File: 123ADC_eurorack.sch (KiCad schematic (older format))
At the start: 78 parts, among them J1 CLOCK_IN, J10 BIT_7, J11 Conn_01x06_Male, J12 Conn_01x06_Female, J13 Conn_01x06_Male, J14 Conn_01x06_Female, J15 Conn_02x05_Odd_Even, J2 CV_IN, J3 BIT_0, J4 BIT_1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

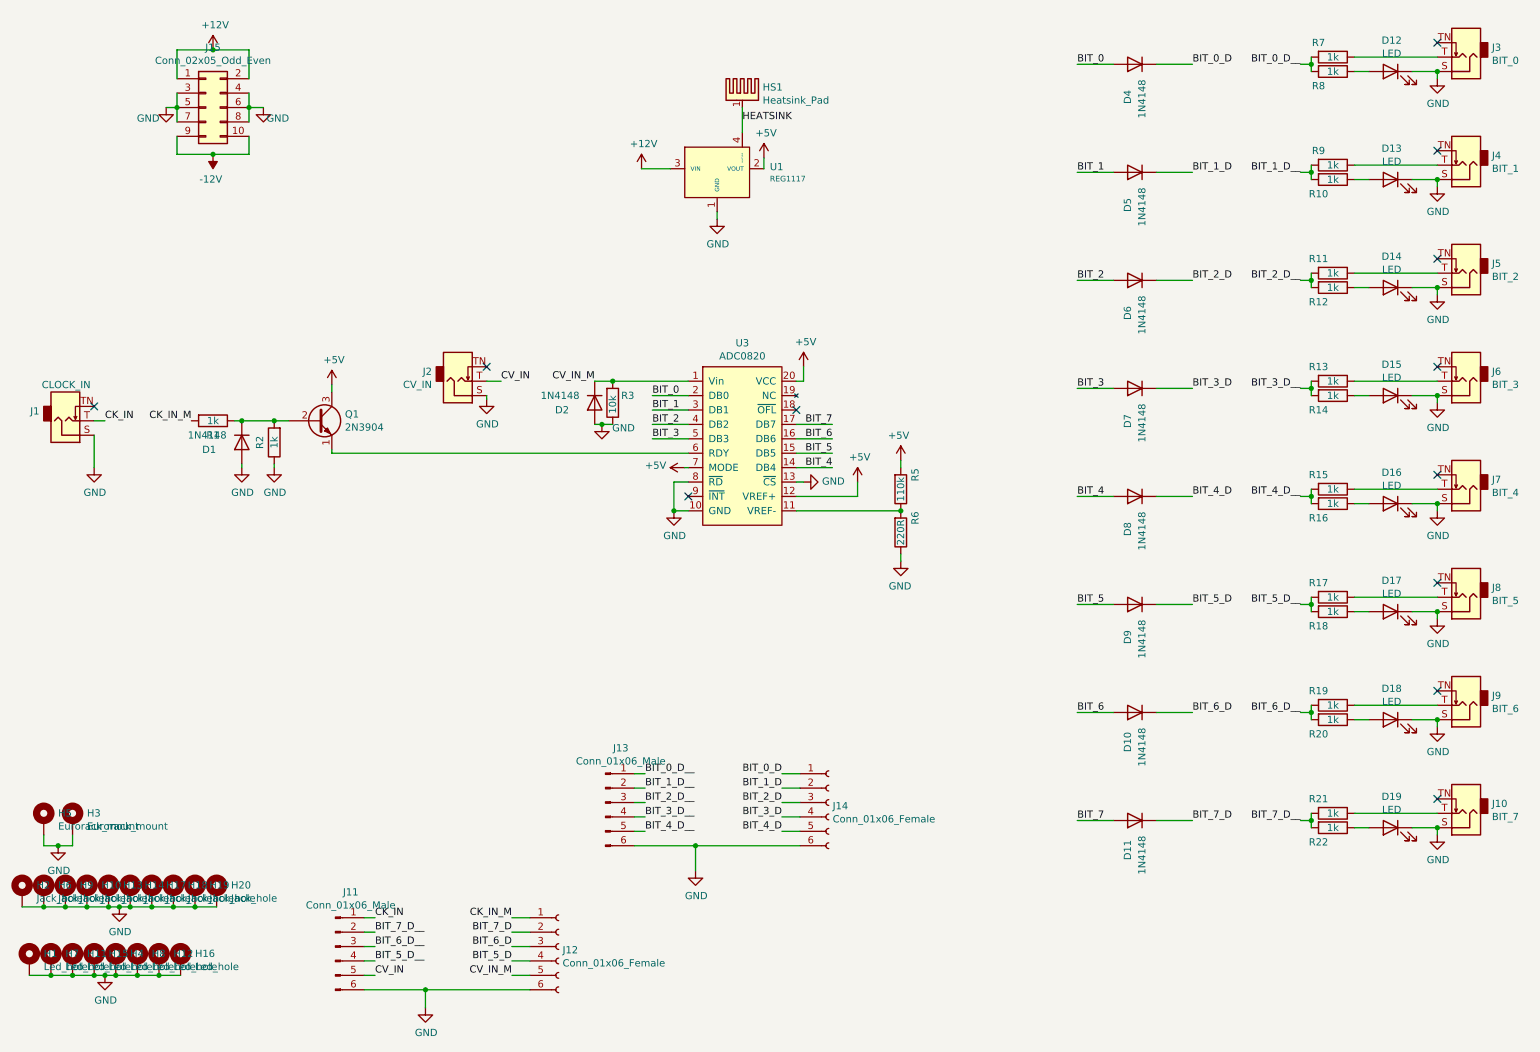
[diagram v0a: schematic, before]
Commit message: :sparkles: Add reverse power protection and power conditioning caps
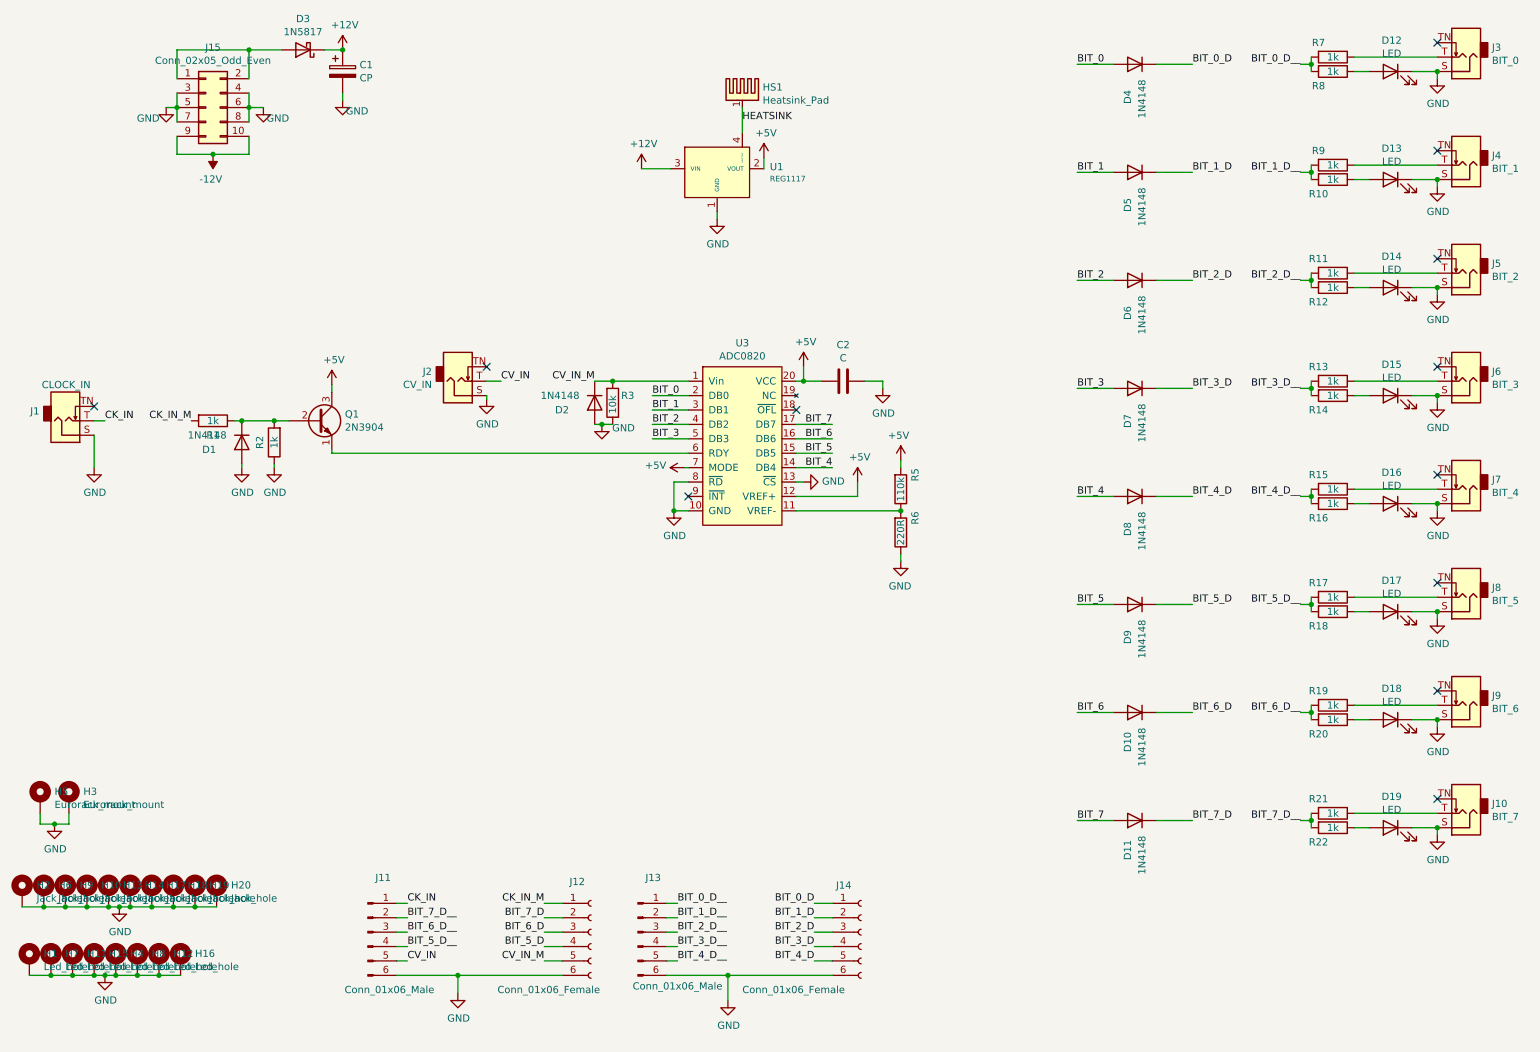
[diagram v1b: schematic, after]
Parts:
- added C1: CP, Capacitor_THT:CP_Radial_D5.0mm_P2.50mm, symbol Device:CP
- added C2: C, Capacitor_THT:C_Disc_D3.8mm_W2.6mm_P2.50mm, symbol Device:C
- added D3: 1N5817, Diode_THT:D_DO-41_SOD81_P10.16mm_Horizontal, symbol Diode:1N5817
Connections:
- net +12V: now also C1.1, D3.1 (K); no longer J15.1 (Pin_1), J15.2 (Pin_2)
- net +5V: now also C2.2
- net GND: now also C1.2, C2.1
- new net: D3.2 (A), J15.1 (Pin_1), J15.2 (Pin_2)
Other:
- moved on the sheet: H3, H5, J11, J12, J13, J14

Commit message: :bug: Fix resistor values
same
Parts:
- C1: symbol Device:CP -> 123ADC_eurorack-rescue:CP-Device
- Q1: footprint Package_TO_SOT_THT:TO-92_Inline -> Package_TO_SOT_THT:TO-92_Inline_Wide
- R10, R12, R14, R16, R18, R2, R20, R22, R8: value 1k -> 10k
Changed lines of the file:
@@
 EESchema Schematic File Version 4
-EELAYER 26 0
+EELAYER 30 0
 EELAYER END
 $Descr A4 11693 8268
@@
 P 9725 1675
 F 0 "R10" V 9825 1575 50  0000 C CNN
-F 1 "1k" V 9725 1675 50  0000 C CNN
+F 1 "10k" V 9725 1675 50  0000 C CNN
 F 2 "Resistor_THT:R_Axial_DIN0207_L6.3mm_D2.5mm_P7.62mm_Horizontal" V 9655 1675 50  0001 C CNN
 F 3 "~" H 9725 1675 50  0001 C CNN
@@
 F 0 "Q1" H 2866 3396 50  0000 L CNN
 F 1 "2N3904" H 2866 3305 50  0000 L CNN
-F 2 "Package_TO_SOT_THT:TO-92_Inline" H 2875 3275 50  0001 L CIN
+F 2 "Package_TO_SOT_THT:TO-92_Inline_Wide" H 2875 3275 50  0001 L CIN
 F 3 "https://www.fairchildsemi.com/datasheets/2N/2N3904.pdf" H 2675 3350 50  0001 L CNN
 	1    2675 3350
@@
 P 2150 3500
 F 0 "D1" V 2200 3775 50  0000 R CNN
-F 1 "1N4148" V 2100 3875 50  0000 R CNN
+F 1 "1N4148" V 2325 3875 50  0000 R CNN
 F 2 "Diode_THT:D_DO-35_SOD27_P7.62mm_Horizontal" H 2150 3325 50  0001 C CNN
 F 3 "https://assets.nexperia.com/documents/data-sheet/1N4148_1N4448.pdf" H 2150 3500 50  0001 C CNN
@@
 P 2375 3500
 F 0 "R2" V 2475 3500 50  0000 C CNN
-F 1 "1k" V 2375 3500 50  0000 C CNN
+F 1 "10k" V 2375 3500 50  0000 C CNN
 F 2 "Resistor_THT:R_Axial_DIN0207_L6.3mm_D2.5mm_P7.62mm_Horizontal" V 2305 3500 50  0001 C CNN
 F 3 "~" H 2375 3500 50  0001 C CNN
@@
 P 9725 2425
 F 0 "R12" V 9825 2325 50  0000 C CNN
-F 1 "1k" V 9725 2425 50  0000 C CNN
+F 1 "10k" V 9725 2425 50  0000 C CNN
 F 2 "Resistor_THT:R_Axial_DIN0207_L6.3mm_D2.5mm_P7.62mm_Horizontal" V 9655 2425 50  0001 C CNN
 F 3 "~" H 9725 2425 50  0001 C CNN
@@
 P 9725 3175
 F 0 "R14" V 9825 3075 50  0000 C CNN
-F 1 "1k" V 9725 3175 50  0000 C CNN
+F 1 "10k" V 9725 3175 50  0000 C CNN
 F 2 "Resistor_THT:R_Axial_DIN0207_L6.3mm_D2.5mm_P7.62mm_Horizontal" V 9655 3175 50  0001 C CNN
 F 3 "~" H 9725 3175 50  0001 C CNN
@@
 P 9725 3925
 F 0 "R16" V 9825 3825 50  0000 C CNN
-F 1 "1k" V 9725 3925 50  0000 C CNN
+F 1 "10k" V 9725 3925 50  0000 C CNN
 F 2 "Resistor_THT:R_Axial_DIN0207_L6.3mm_D2.5mm_P7.62mm_Horizontal" V 9655 3925 50  0001 C CNN
 F 3 "~" H 9725 3925 50  0001 C CNN
@@
 P 9725 4675
 F 0 "R18" V 9825 4575 50  0000 C CNN
-F 1 "1k" V 9725 4675 50  0000 C CNN
+F 1 "10k" V 9725 4675 50  0000 C CNN
 F 2 "Resistor_THT:R_Axial_DIN0207_L6.3mm_D2.5mm_P7.62mm_Horizontal" V 9655 4675 50  0001 C CNN
 F 3 "~" H 9725 4675 50  0001 C CNN
@@
 P 9725 5425
 F 0 "R20" V 9825 5325 50  0000 C CNN
-F 1 "1k" V 9725 5425 50  0000 C CNN
+F 1 "10k" V 9725 5425 50  0000 C CNN
 F 2 "Resistor_THT:R_Axial_DIN0207_L6.3mm_D2.5mm_P7.62mm_Horizontal" V 9655 5425 50  0001 C CNN
 F 3 "~" H 9725 5425 50  0001 C CNN
@@
 P 9725 6175
 F 0 "R22" V 9825 6075 50  0000 C CNN
-F 1 "1k" V 9725 6175 50  0000 C CNN
+F 1 "10k" V 9725 6175 50  0000 C CNN
 F 2 "Resistor_THT:R_Axial_DIN0207_L6.3mm_D2.5mm_P7.62mm_Horizontal" V 9655 6175 50  0001 C CNN
 F 3 "~" H 9725 6175 50  0001 C CNN
@@
 P 9725 925
 F 0 "R8" V 9825 825 50  0000 C CNN
-F 1 "1k" V 9725 925 50  0000 C CNN
+F 1 "10k" V 9725 925 50  0000 C CNN
 F 2 "Resistor_THT:R_Axial_DIN0207_L6.3mm_D2.5mm_P7.62mm_Horizontal" V 9655 925 50  0001 C CNN
 F 3 "~" H 9725 925 50  0001 C CNN
@@
 	6600 3075 6600 3125
 $Comp
-L Device:CP C1
+L 123ADC_eurorack-rescue:CP-Device C1
 U 1 1 5E574C33
 P 2850 925
